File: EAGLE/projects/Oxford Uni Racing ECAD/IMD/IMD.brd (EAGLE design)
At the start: 59.7 x 44.5 mm, 6 parts, among them IC1 LM2901N, K1 RT444012, T1 BT169

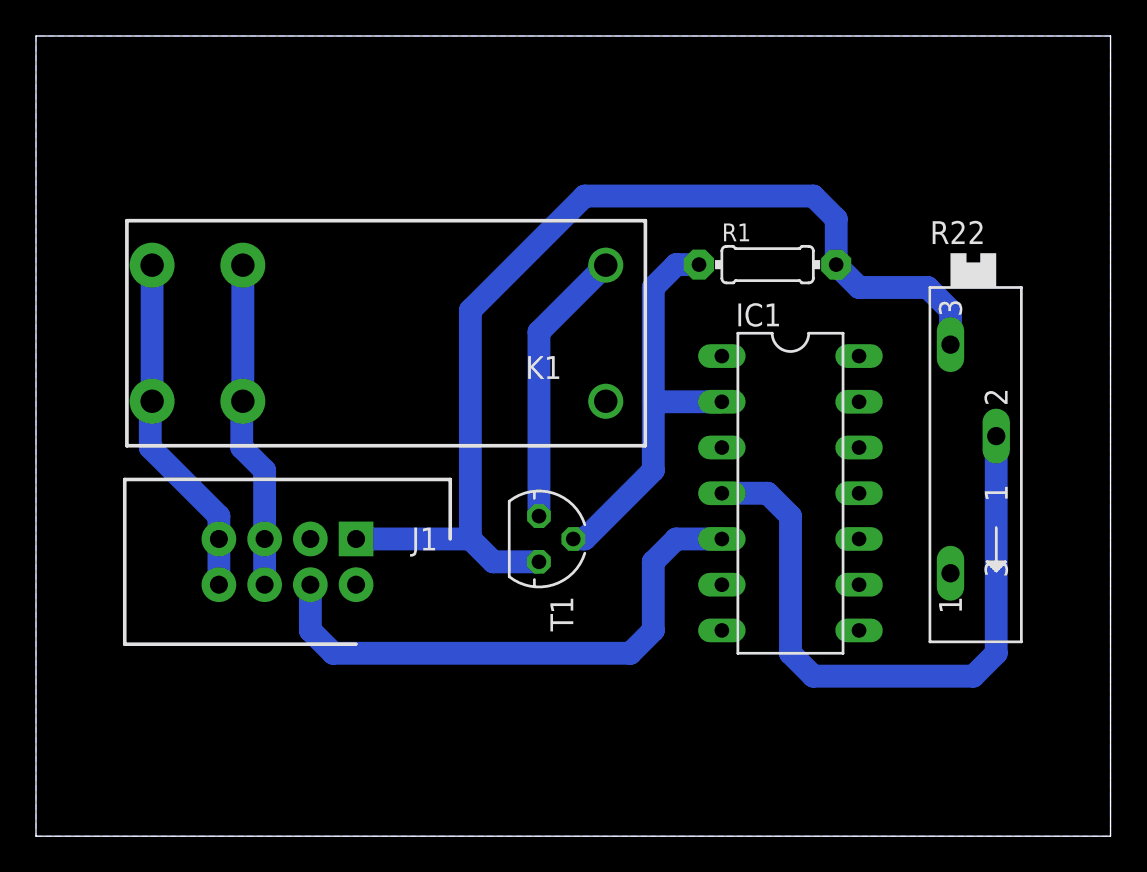
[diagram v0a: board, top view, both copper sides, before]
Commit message: fixed IMD with a MOSFET rather than a thyristor
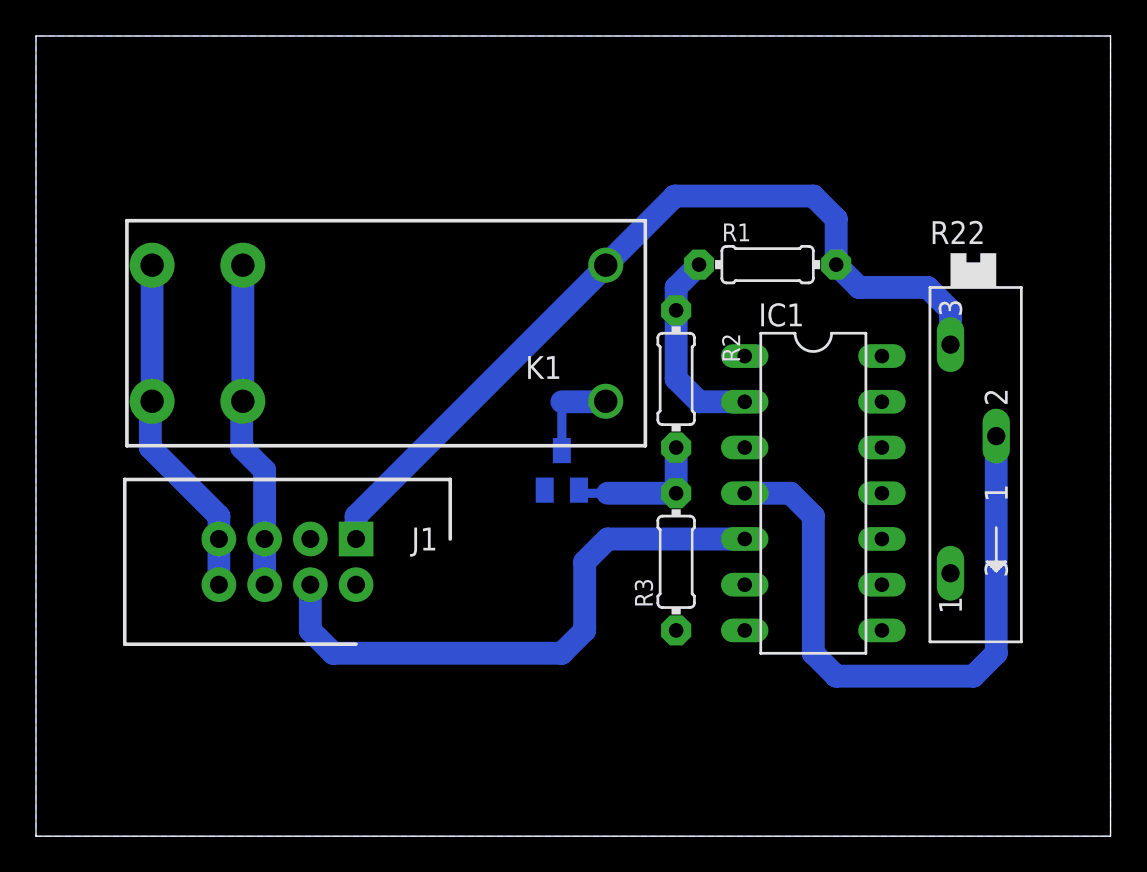
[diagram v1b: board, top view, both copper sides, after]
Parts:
- removed T1: BT169, triac:TO92-2
- added BR_LIGHTS_TR: IRLML2502GTRPBF, adafruit:SOT23
- added R2: 1K, adafruit:0204/7
- added R3: 47K, adafruit:0204/7
- R1: value 47K -> 1K
- moved IC1 1.27 mm to (43.2, 19.1)
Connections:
- new net N$6: BR_LIGHTS_TR.3, K1.A2
- net 12V: now also K1.A1; no longer T1.A
- net GND: now also BR_LIGHTS_TR.2, R3.1; no longer K1.A2
- net N$1: now also R2.1; no longer T1.G
- net N$3: now also BR_LIGHTS_TR.1, R2.2, R3.2; no longer K1.A1, T1.C
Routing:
- net N$1: track 23.1 -> 11.2 mm
- net 12V: track 58.7 -> 47.7 mm
- net N$3: track 15.5 -> 8.01 mm
- net N$6: track 0.00 -> 5.16 mm
- net N$4: track 36.5 -> 35.2 mm
- net IMD_REF: track 30.8 -> 32.1 mm
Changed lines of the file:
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@@
 </autorouter>
 <elements>
-<element name="IC1" library="linear" library_urn="urn:adsk.eagle:library:262" package="DIL14" package3d_urn="urn:adsk.eagle:package:16407/2" value="LM2901N" x="41.91" y="19.05" smashed="yes" rot="R270">
-<attribute name="NAME" x="38.862" y="28.321" size="1.27" layer="25" ratio="10"/>
-<attribute name="VALUE" x="41.275" y="25.781" size="1.27" layer="27" ratio="10" rot="R270"/>
+<element name="IC1" library="linear" library_urn="urn:adsk.eagle:library:262" package="DIL14" package3d_urn="urn:adsk.eagle:package:16407/2" value="LM2901N" x="43.18" y="19.05" smashed="yes" rot="R270">
+<attribute name="NAME" x="40.132" y="28.321" size="1.27" layer="25" ratio="10"/>
+<attribute name="VALUE" x="42.545" y="25.781" size="1.27" layer="27" ratio="10" rot="R270"/>
 </element>
 <element name="J1" library="T821108A1S100CEU" package="HDRV8W64P254_2X4_1778X895X915P" value="" x="17.78" y="16.51" smashed="yes" rot="R180">
@@
 <attribute name="VALUE" x="29.21" y="29.21" size="1.27" layer="27" rot="R180"/>
 </element>
-<element name="R1" library="adafruit" library_urn="urn:adsk.eagle:library:420" package="0204/7" package3d_urn="urn:adsk.eagle:package:6240596/1" value="47K" x="40.64" y="31.75" smashed="yes">
+<element name="R1" library="adafruit" library_urn="urn:adsk.eagle:library:420" package="0204/7" package3d_urn="urn:adsk.eagle:package:6240596/1" value="1K" x="40.64" y="31.75" smashed="yes">
 <attribute name="NAME" x="38.1" y="33.0454" size="0.9906" layer="25" ratio="12"/>
 <attribute name="VALUE" x="39.0144" y="31.2674" size="0.9906" layer="27" ratio="12"/>
@@
 <attribute name="VALUE" x="50.292" y="24.765" size="1.27" layer="27" ratio="10" rot="R270"/>
 </element>
-<element name="T1" library="triac" library_urn="urn:adsk.eagle:library:403" package="TO92-2" package3d_urn="urn:adsk.eagle:package:30142/1" value="BT169" x="27.94" y="16.51" smashed="yes" rot="R270">
-<attribute name="NAME" x="28.575" y="13.335" size="1.27" layer="25" ratio="10" rot="R270"/>
-<attribute name="VALUE" x="26.67" y="13.335" size="1.27" layer="27" ratio="10" rot="R270"/>
+<element name="BR_LIGHTS_TR" library="adafruit" library_urn="urn:adsk.eagle:library:420" package="SOT23" package3d_urn="urn:adsk.eagle:package:6240836/1" value="IRLML2502GTRPBF" x="29.21" y="20.32" smashed="yes" rot="MR0">
+<attribute name="NAME" x="31.115" y="22.225" size="1.27" layer="26" rot="MR0"/>
+<attribute name="VALUE" x="31.115" y="17.145" size="1.27" layer="28" rot="MR0"/>
+</element>
+<element name="R2" library="adafruit" library_urn="urn:adsk.eagle:library:420" package="0204/7" package3d_urn="urn:adsk.eagle:package:6240596/1" value="1K" x="35.56" y="25.4" smashed="yes" rot="R270">
+<attribute name="NAME" x="38.1254" y="27.94" size="0.9906" layer="25" ratio="12" rot="R270"/>
+<attribute name="VALUE" x="35.0774" y="27.0256" size="0.9906" layer="27" ratio="12" rot="R270"/>
+</element>
+<element name="R3" library="adafruit" library_urn="urn:adsk.eagle:library:420" package="0204/7" package3d_urn="urn:adsk.eagle:package:6240596/1" value="47K" x="35.56" y="15.24" smashed="yes" rot="R90">
+<attribute name="NAME" x="34.2646" y="12.7" size="0.9906" layer="25" ratio="12" rot="R90"/>
+<attribute name="VALUE" x="36.0426" y="13.6144" size="0.9906" layer="27" ratio="12" rot="R90"/>
 </element>
 </elements>
@@
 <contactref element="IC1" pad="11"/>
 <contactref element="IC1" pad="8"/>
-<contactref element="K1" pad="A2"/>
 <contactref element="J1" pad="2"/>
 <contactref element="R22" pad="A"/>
@@
 <vertex x="0" y="44.45"/>
 </polygon>
+<contactref element="BR_LIGHTS_TR" pad="2"/>
+<contactref element="R3" pad="1"/>
 </signal>
 <signal name="N$1">
 <contactref element="IC1" pad="2"/>
-<contactref element="T1" pad="G"/>
 <contactref element="R1" pad="1"/>
-<wire x1="29.845" y1="16.51" x2="30.48" y2="16.51" width="1.27" layer="16"/>
-<wire x1="30.48" y1="16.51" x2="34.29" y2="20.32" width="1.27" layer="16"/>
-<wire x1="34.29" y1="30.48" x2="35.56" y2="31.75" width="1.27" layer="16"/>
-<wire x1="35.56" y1="31.75" x2="36.83" y2="31.75" width="1.27" layer="16"/>
-<wire x1="34.29" y1="20.32" x2="34.29" y2="24.13" width="1.27" layer="16"/>
-<wire x1="34.29" y1="24.13" x2="34.29" y2="30.48" width="1.27" layer="16"/>
-<wire x1="38.1" y1="24.13" x2="34.29" y2="24.13" width="1.27" layer="16"/>
+<contactref element="R2" pad="1"/>
+<wire x1="36.83" y1="31.75" x2="35.56" y2="30.48" width="1.27" layer="16"/>
+<wire x1="35.56" y1="30.48" x2="35.56" y2="29.21" width="1.27" layer="16"/>
+<wire x1="39.37" y1="24.13" x2="36.83" y2="24.13" width="1.27" layer="16"/>
+<wire x1="36.83" y1="24.13" x2="35.56" y2="25.4" width="1.27" layer="16"/>
+<wire x1="35.56" y1="25.4" x2="35.56" y2="29.21" width="1.27" layer="16"/>
 </signal>
 <signal name="12V">
 <contactref element="R1" pad="2"/>
-<contactref element="T1" pad="A"/>
 <contactref element="J1" pad="1"/>
 <contactref element="R22" pad="E"/>
-<wire x1="17.78" y1="16.51" x2="24.13" y2="16.51" width="1.27" layer="16"/>
-<wire x1="24.13" y1="16.51" x2="25.4" y2="15.24" width="1.27" layer="16"/>
-<wire x1="25.4" y1="15.24" x2="27.94" y2="15.24" width="1.27" layer="16"/>
-<wire x1="24.13" y1="16.51" x2="24.13" y2="29.21" width="1.27" layer="16"/>
-<wire x1="24.13" y1="29.21" x2="30.48" y2="35.56" width="1.27" layer="16"/>
 <wire x1="43.18" y1="35.56" x2="44.45" y2="34.29" width="1.27" layer="16"/>
 <wire x1="44.45" y1="34.29" x2="44.45" y2="31.75" width="1.27" layer="16"/>
-<wire x1="30.48" y1="35.56" x2="43.18" y2="35.56" width="1.27" layer="16"/>
 <wire x1="44.45" y1="31.75" x2="45.72" y2="30.48" width="1.27" layer="16"/>
 <wire x1="49.53" y1="30.48" x2="50.8" y2="29.21" width="1.27" layer="16"/>
 <wire x1="50.8" y1="29.21" x2="50.8" y2="27.305" width="1.27" layer="16"/>
 <wire x1="45.72" y1="30.48" x2="49.53" y2="30.48" width="1.27" layer="16"/>
-</signal>
-<signal name="N$3">
-<contactref element="T1" pad="C"/>
 <contactref element="K1" pad="A1"/>
-<wire x1="27.94" y1="28.01" x2="31.65" y2="31.72" width="1.27" layer="16"/>
-<wire x1="27.94" y1="17.78" x2="27.94" y2="28.01" width="1.27" layer="16"/>
+<wire x1="17.78" y1="16.51" x2="17.78" y2="17.78" width="1.27" layer="16"/>
+<wire x1="31.65" y1="31.72" x2="31.65" y2="31.65" width="1.27" layer="16"/>
+<wire x1="31.65" y1="31.65" x2="17.78" y2="17.78" width="1.27" layer="16"/>
+<wire x1="31.65" y1="31.72" x2="35.49" y2="35.56" width="1.27" layer="16"/>
+<wire x1="35.49" y1="35.56" x2="43.18" y2="35.56" width="1.27" layer="16"/>
 </signal>
 <signal name="ASS1">
@@
 <wire x1="53.34" y1="22.225" x2="53.34" y2="10.16" width="1.27" layer="16"/>
 <wire x1="53.34" y1="10.16" x2="52.07" y2="8.89" width="1.27" layer="16"/>
-<wire x1="52.07" y1="8.89" x2="43.18" y2="8.89" width="1.27" layer="16"/>
-<wire x1="43.18" y1="8.89" x2="41.91" y2="10.16" width="1.27" layer="16"/>
-<wire x1="41.91" y1="10.16" x2="41.91" y2="17.78" width="1.27" layer="16"/>
-<wire x1="41.91" y1="17.78" x2="40.64" y2="19.05" width="1.27" layer="16"/>
-<wire x1="40.64" y1="19.05" x2="38.1" y2="19.05" width="1.27" layer="16"/>
+<wire x1="52.07" y1="8.89" x2="44.45" y2="8.89" width="1.27" layer="16"/>
+<wire x1="44.45" y1="8.89" x2="43.18" y2="10.16" width="1.27" layer="16"/>
+<wire x1="43.18" y1="10.16" x2="43.18" y2="17.78" width="1.27" layer="16"/>
+<wire x1="43.18" y1="17.78" x2="41.91" y2="19.05" width="1.27" layer="16"/>
+<wire x1="41.91" y1="19.05" x2="39.37" y2="19.05" width="1.27" layer="16"/>
 </signal>
 <signal name="IMD_REF">
@@
 <wire x1="15.24" y1="13.97" x2="15.24" y2="11.43" width="1.27" layer="16"/>
 <wire x1="15.24" y1="11.43" x2="16.51" y2="10.16" width="1.27" layer="16"/>
-<wire x1="33.02" y1="10.16" x2="34.29" y2="11.43" width="1.27" layer="16"/>
-<wire x1="34.29" y1="15.24" x2="35.56" y2="16.51" width="1.27" layer="16"/>
-<wire x1="35.56" y1="16.51" x2="38.1" y2="16.51" width="1.27" layer="16"/>
-<wire x1="16.51" y1="10.16" x2="33.02" y2="10.16" width="1.27" layer="16"/>
-<wire x1="34.29" y1="11.43" x2="34.29" y2="15.24" width="1.27" layer="16"/>
+<wire x1="29.21" y1="10.16" x2="30.48" y2="11.43" width="1.27" layer="16"/>
+<wire x1="30.48" y1="15.24" x2="31.75" y2="16.51" width="1.27" layer="16"/>
+<wire x1="31.75" y1="16.51" x2="39.37" y2="16.51" width="1.27" layer="16"/>
+<wire x1="16.51" y1="10.16" x2="29.21" y2="10.16" width="1.27" layer="16"/>
+<wire x1="30.48" y1="11.43" x2="30.48" y2="15.24" width="1.27" layer="16"/>
+</signal>
+<signal name="N$3">
+<contactref element="R2" pad="2"/>
+<contactref element="BR_LIGHTS_TR" pad="1"/>
+<contactref element="R3" pad="2"/>
+<wire x1="35.56" y1="21.59" x2="35.56" y2="19.05" width="1.27" layer="16"/>
+<wire x1="31.75" y1="19.05" x2="35.56" y2="19.05" width="1.27" layer="16"/>
+<wire x1="30.16" y1="19.22" x2="30.33" y2="19.05" width="0.508" layer="16"/>
+<wire x1="30.33" y1="19.05" x2="31.75" y2="19.05" width="0.508" layer="16"/>
+</signal>
+<signal name="N$6">
+<contactref element="BR_LIGHTS_TR" pad="3"/>
+<contactref element="K1" pad="A2"/>
+<wire x1="31.65" y1="24.16" x2="31.62" y2="24.13" width="1.27" layer="16"/>
+<wire x1="29.21" y1="24.13" x2="31.62" y2="24.13" width="1.27" layer="16"/>
+<wire x1="29.21" y1="21.42" x2="29.21" y2="24.13" width="0.508" layer="16"/>
 </signal>
 </signals>

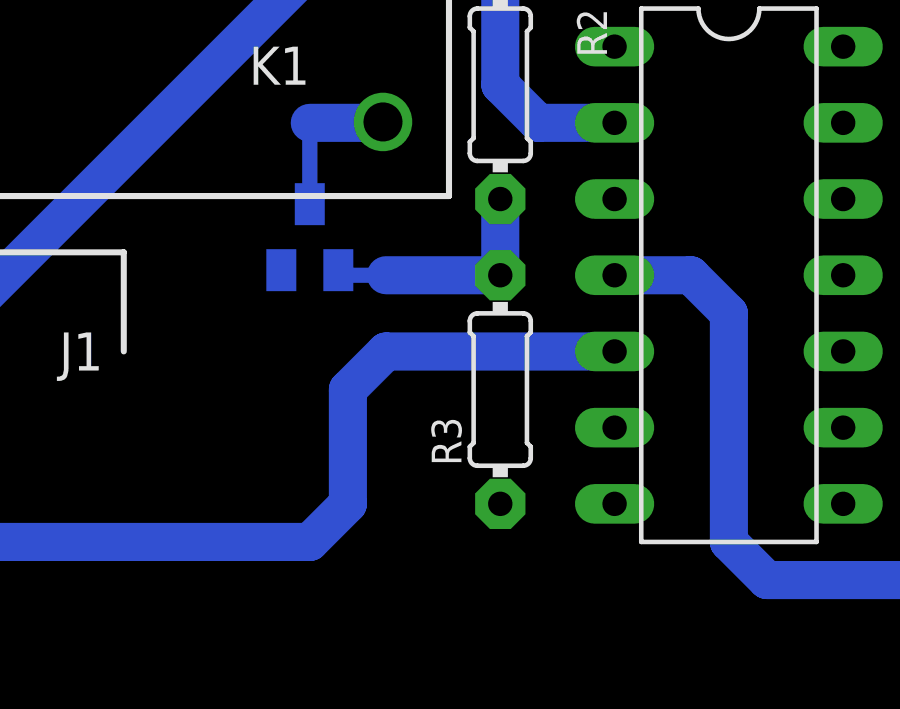
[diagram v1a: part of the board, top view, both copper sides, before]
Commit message: removed unnecessary pulldown resistors
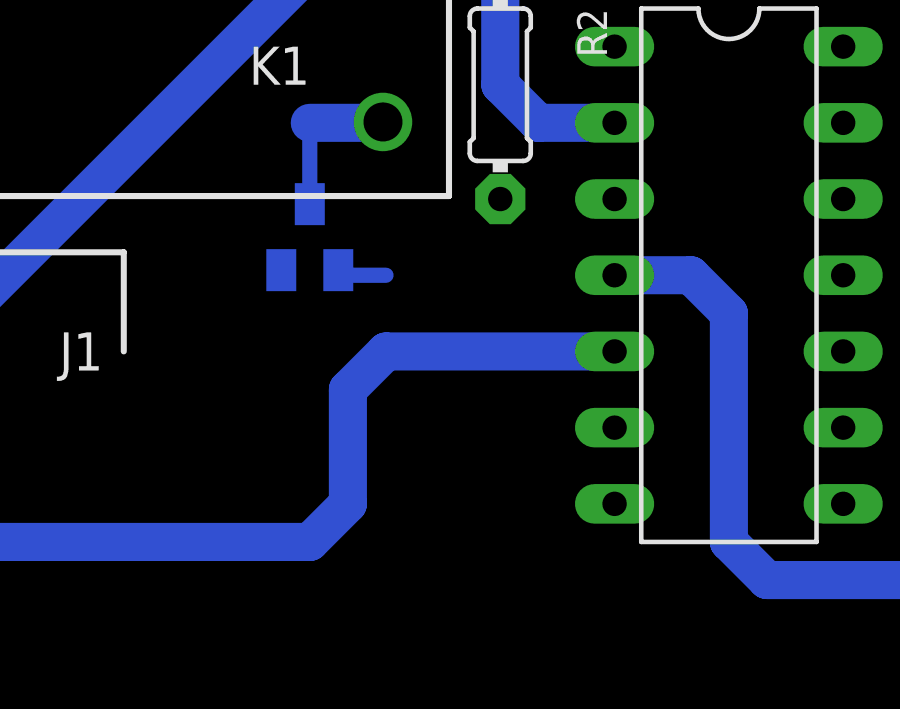
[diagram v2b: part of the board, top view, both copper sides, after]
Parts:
- removed R3: 47K, adafruit:0204/7
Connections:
- net GND: no longer R3.1
- net N$3: no longer R3.2
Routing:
- net N$3: track 8.01 -> 1.66 mm
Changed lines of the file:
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@@
 <attribute name="VALUE" x="35.0774" y="27.0256" size="0.9906" layer="27" ratio="12" rot="R270"/>
-</element>
-<element name="R3" library="adafruit" library_urn="urn:adsk.eagle:library:420" package="0204/7" package3d_urn="urn:adsk.eagle:package:6240596/1" value="47K" x="35.56" y="15.24" smashed="yes" rot="R90">
-<attribute name="NAME" x="34.2646" y="12.7" size="0.9906" layer="25" ratio="12" rot="R90"/>
-<attribute name="VALUE" x="36.0426" y="13.6144" size="0.9906" layer="27" ratio="12" rot="R90"/>
 </element>
 </elements>
@@
 </polygon>
 <contactref element="BR_LIGHTS_TR" pad="2"/>
-<contactref element="R3" pad="1"/>
+<wire x1="46.99" y1="16.51" x2="46.99" y2="19.05" width="0" layer="19" extent="1-1"/>
+<wire x1="46.99" y1="13.97" x2="46.99" y2="16.51" width="0" layer="19" extent="1-1"/>
+<wire x1="46.99" y1="11.43" x2="46.99" y2="13.97" width="0" layer="19" extent="1-1"/>
+<wire x1="50.8" y1="14.605" x2="46.99" y2="13.97" width="0" layer="19" extent="1-1"/>
+<wire x1="39.37" y1="13.97" x2="46.99" y2="13.97" width="0" layer="19" extent="1-1"/>
+<wire x1="39.37" y1="11.43" x2="39.37" y2="13.97" width="0" layer="19" extent="1-1"/>
+<wire x1="28.26" y1="19.22" x2="39.37" y2="13.97" width="0" layer="19" extent="16-16"/>
+<wire x1="17.78" y1="13.97" x2="28.26" y2="19.22" width="0" layer="19" extent="16-16"/>
 </signal>
 <signal name="N$1">
@@
 <contactref element="R2" pad="2"/>
 <contactref element="BR_LIGHTS_TR" pad="1"/>
-<contactref element="R3" pad="2"/>
-<wire x1="35.56" y1="21.59" x2="35.56" y2="19.05" width="1.27" layer="16"/>
-<wire x1="31.75" y1="19.05" x2="35.56" y2="19.05" width="1.27" layer="16"/>
 <wire x1="30.16" y1="19.22" x2="30.33" y2="19.05" width="0.508" layer="16"/>
 <wire x1="30.33" y1="19.05" x2="31.75" y2="19.05" width="0.508" layer="16"/>
+<wire x1="31.75" y1="19.05" x2="35.56" y2="21.59" width="0" layer="19" extent="16-16"/>
 </signal>
 <signal name="N$6">
